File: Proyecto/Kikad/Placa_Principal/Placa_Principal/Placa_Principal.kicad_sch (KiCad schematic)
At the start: 8 parts, among them J1 Screw_Terminal_01x03, J2 Screw_Terminal_01x03, J3 Screw_Terminal_01x03, J4 Screw_Terminal_01x03, J5 USB_C_Receptacle_PowerOnly_6P, SW1 SW_DIP_x01, U1 ESP32-DEVKITC-32D

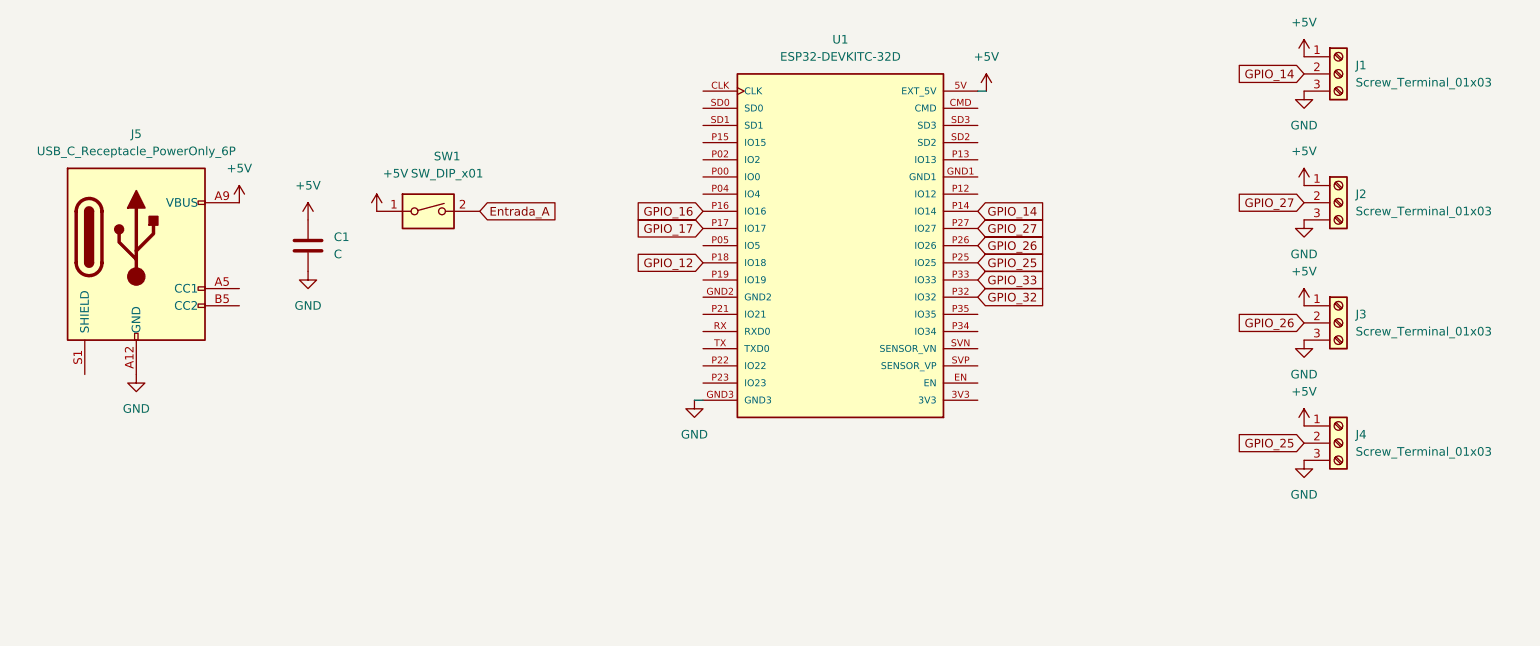
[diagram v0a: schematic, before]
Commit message: Hice la Placa_Principal y corregi algunos detalles de la placa modulo rele
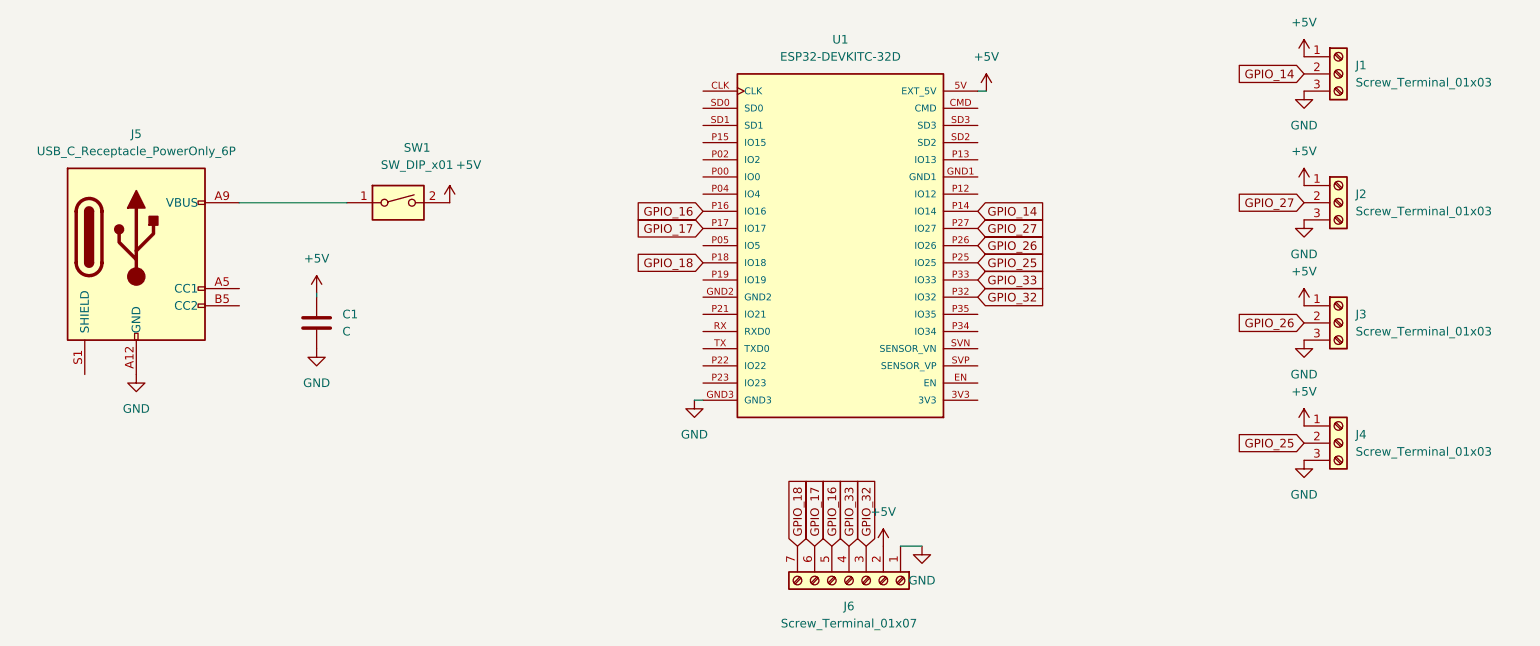
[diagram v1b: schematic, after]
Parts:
- added J6: Screw_Terminal_01x07, Huellas:PinHeader_1x07_P2.54mm_Vertical, symbol Terminal_block_01x07:Screw_Terminal_01x07
- J4: footprint Connector_PinHeader_2.54mm:PinHeader_1x03_P2.54mm_Vertical -> Huellas:PinHeader_1x03_P2.54mm_Vertical
- SW1: footprint Button_Switch_THT:SW_DIP_SPSTx01_Slide_6.7x4.1mm_W7.62mm_P2.54mm_LowProfile -> Huellas:PinHeader_1x03_P2.54mm_Vertical
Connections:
- net Entrada_A is gone; now on net +5V: SW1.2
- net +5V: now also C1.2, J6.2 (Pin_2); no longer C1.1, J5.A9 (VBUS), J5.B9 (VBUS), SW1.1
- net GND: now also C1.1, J6.1 (Pin_1); no longer C1.2
- net GPIO_16: now also J6.5 (Pin_5)
- net GPIO_17: now also J6.6 (Pin_6)
- net GPIO_32: now also J6.3 (Pin_3)
- net GPIO_33: now also J6.4 (Pin_4)
- net GPIO_12 renamed GPIO_18
- net GPIO_18: now also J6.7 (Pin_7)
- new net: J5.A9 (VBUS), J5.B9 (VBUS), SW1.1
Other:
- moved on the sheet: C1, SW1

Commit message: Arregle unas cosas de las dos placas
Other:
- moved on the sheet: SW1
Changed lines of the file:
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@@
 	(wire
 		(pts
-			(xy 82.55 97.79) (xy 98.425 97.79)
+			(xy 82.55 97.79) (xy 86.36 97.79)
 		)
 		(stroke
@@
 	(symbol
 		(lib_id "Switch:SW_DIP_x01")
-		(at 106.045 97.79 0)
+		(at 93.98 97.79 0)
 		(unit 1)
 		(exclude_from_sim no)
@@
 		(dnp no)
 		(property "Reference" "SW1"
-			(at 108.839 89.662 0)
+			(at 96.774 89.662 0)
 			(effects
 				(font
@@
 		)
 		(property "Value" "SW_DIP_x01"
-			(at 108.839 92.202 0)
+			(at 96.774 92.202 0)
 			(effects
 				(font
@@
 		)
 		(property "Footprint" "Huellas:PinHeader_1x03_P2.54mm_Vertical"
-			(at 106.045 97.79 0)
+			(at 93.98 97.79 0)
 			(effects
 				(font
@@
 		)
 		(property "Datasheet" "~"
-			(at 106.045 97.79 0)
+			(at 93.98 97.79 0)
 			(effects
 				(font
@@
 		)
 		(property "Description" "1x DIP Switch, Single Pole Single Throw (SPST) switch, small symbol"
-			(at 106.045 97.79 0)
+			(at 93.98 97.79 0)
 			(effects
 				(font
@@
 	(symbol
 		(lib_id "power:+5V")
-		(at 113.665 97.79 0)
+		(at 101.6 97.79 0)
 		(unit 1)
 		(exclude_from_sim no)
@@
 		(dnp no)
 		(property "Reference" "#PWR03"
-			(at 113.665 101.6 0)
+			(at 101.6 101.6 0)
 			(effects
 				(font
@@
 		)
 		(property "Value" "+5V"
-			(at 116.459 92.202 0)
+			(at 104.394 92.202 0)
 			(effects
 				(font
@@
 		)
 		(property "Footprint" ""
-			(at 113.665 97.79 0)
+			(at 101.6 97.79 0)
 			(effects
 				(font
@@
 		)
 		(property "Datasheet" ""
-			(at 113.665 97.79 0)
+			(at 101.6 97.79 0)
 			(effects
 				(font
@@
 		)
 		(property "Description" "Power symbol creates a global label with name \"+5V\""
-			(at 113.665 97.79 0)
-			(effects
-				(font
+			(at 101.6 97.79 0)
+			(effects
+				(font
